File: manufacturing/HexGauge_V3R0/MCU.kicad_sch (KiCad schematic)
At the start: 18 parts, among them SW1 SW_SPDT, U2 STM32F405RGT6, Y1 25MHz 12pF

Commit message: Updated Board and added Images
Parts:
- added D2: White, LED_SMD:LED_0603_1608Metric, symbol Device:LED
- added R1: 1k5, Resistor_SMD:R_0402_1005Metric, symbol Device:R
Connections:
- net GND: now also D2.1 (K)
- net TFT_CS: now also U2.24 (PC4); no longer U2.22 (PA6)
- net TFT_DC: now also U2.20 (PA4); no longer U2.24 (PC4)
- net TFT_RST: now also U2.22 (PA6); no longer U2.20 (PA4)
- net SD_DAT1: now reaches U2.54 (PD2)
- net SD_DAT3: now reaches U2.56 (PB4)
- net SD_DAT2: now reaches U2.57 (PB5)
- net DEBUG_LED: now reaches U2.58 (PB6)
- net DEBUG_LED: now also R1.2
- net SD_CS renamed SD_DET
- net SD_MISO renamed SD_DAT0
- net SD_MOSI renamed SD_CMD
- net SD_SCK renamed SD_CLK
- new net: D2.2 (A), R1.1
- no-connect marks 29 -> 26
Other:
- note added: "CS"
- note added: "MISO"
- note added: "MOSI"
- note added: "SCK"
- moved on the sheet: C10, C9

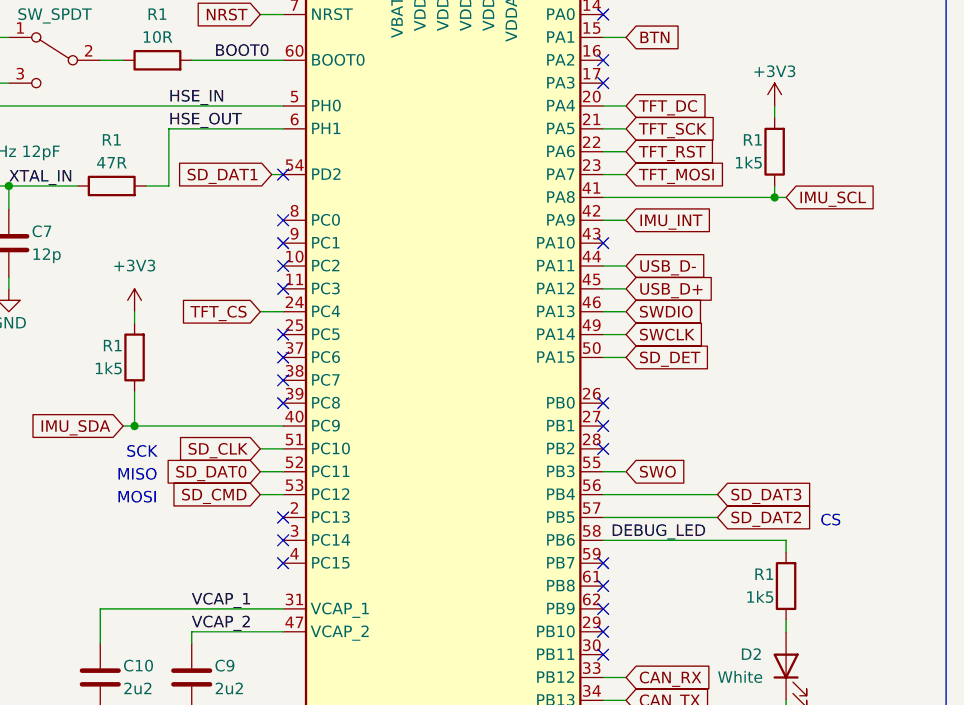
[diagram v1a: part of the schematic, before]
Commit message: V3R0 SPI SD Card Update
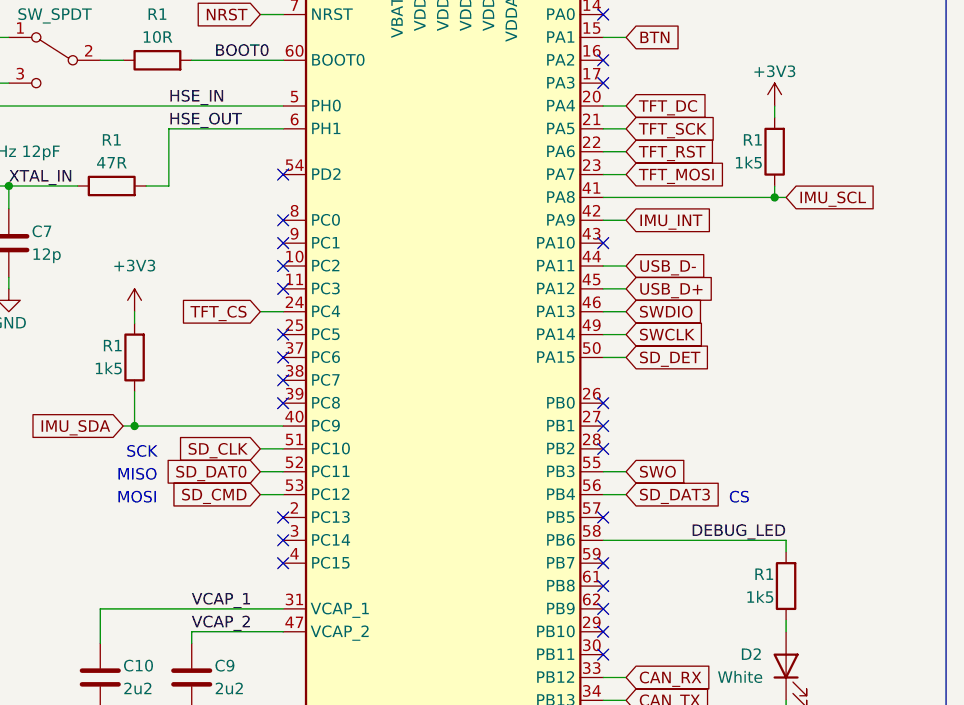
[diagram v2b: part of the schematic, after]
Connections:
- net SD_DAT1: no longer names the net of U2.54 (PD2)
- net SD_DAT2: no longer names the net of U2.57 (PB5)
- no-connect marks 26 -> 27
